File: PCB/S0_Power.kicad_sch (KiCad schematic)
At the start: 9 parts, among them J5 PJ-102BH, U10 LM2576HVS-5, U13 TLV76133DCY

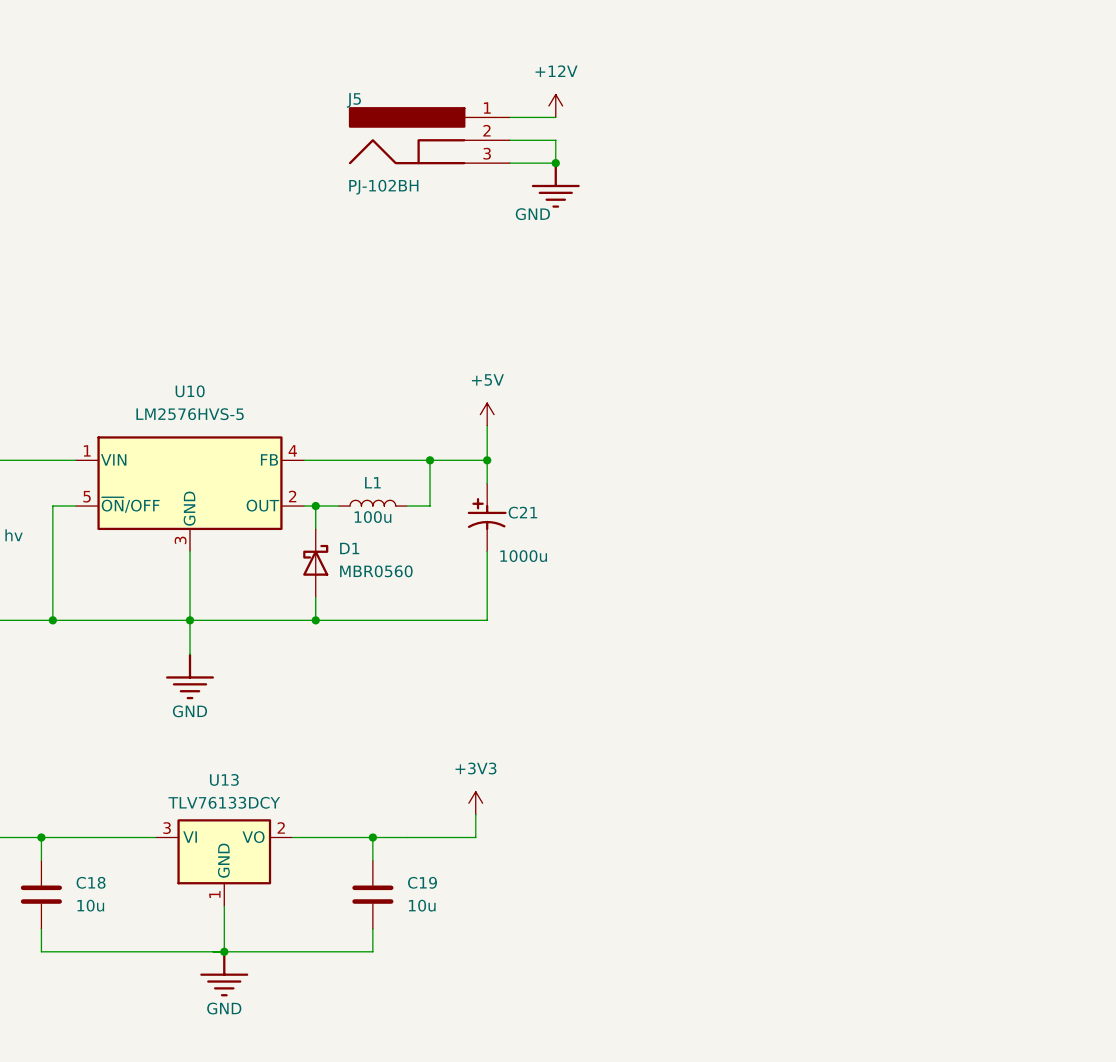
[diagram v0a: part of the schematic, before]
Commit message: Update PCB to seperate ground symbols apporiately. Modify board to sepearte ground path for motor current and all other devices. Add filtering for slide power, hopefully reduce bownout or other issue.
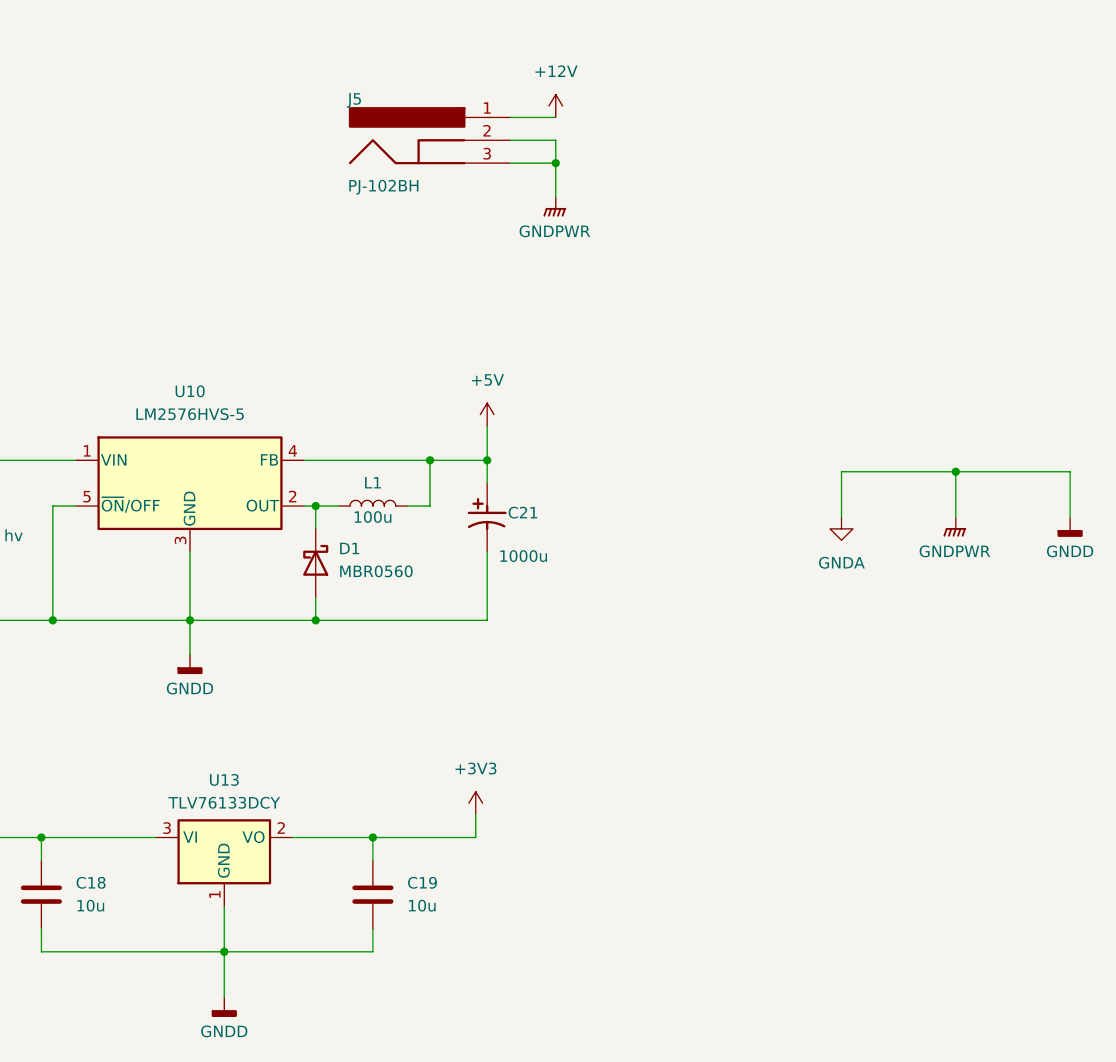
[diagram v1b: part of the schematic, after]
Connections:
- net GND renamed GNDA

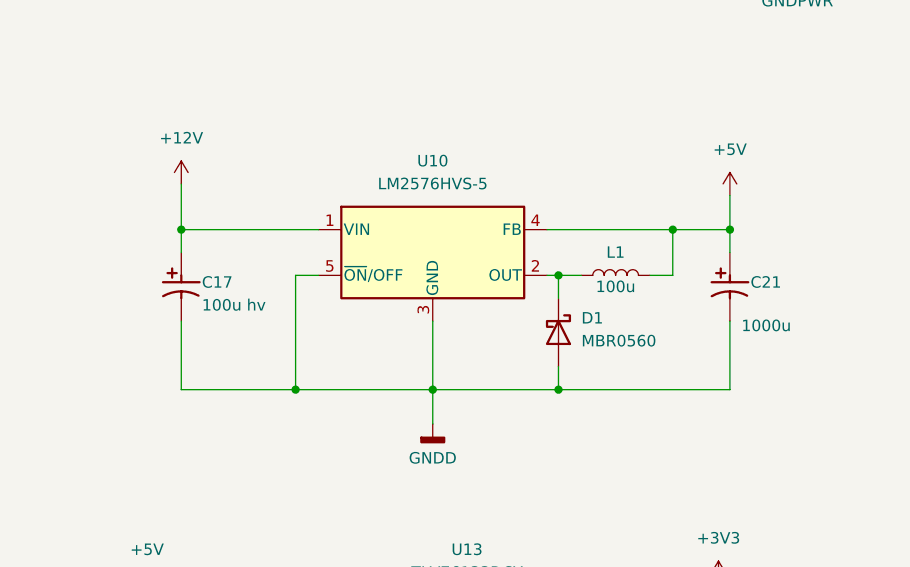
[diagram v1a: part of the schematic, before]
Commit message: WIP Adding adudino onboard, so far copying pro mega
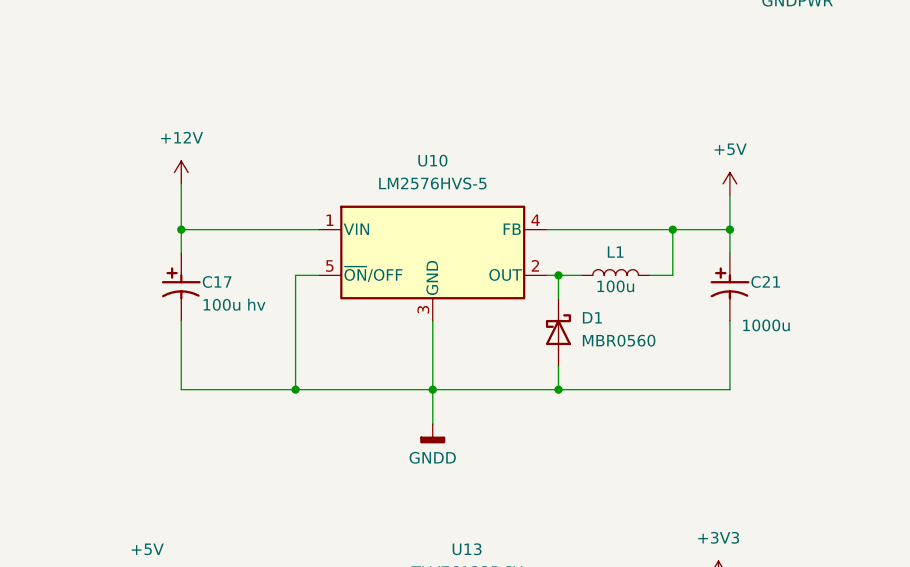
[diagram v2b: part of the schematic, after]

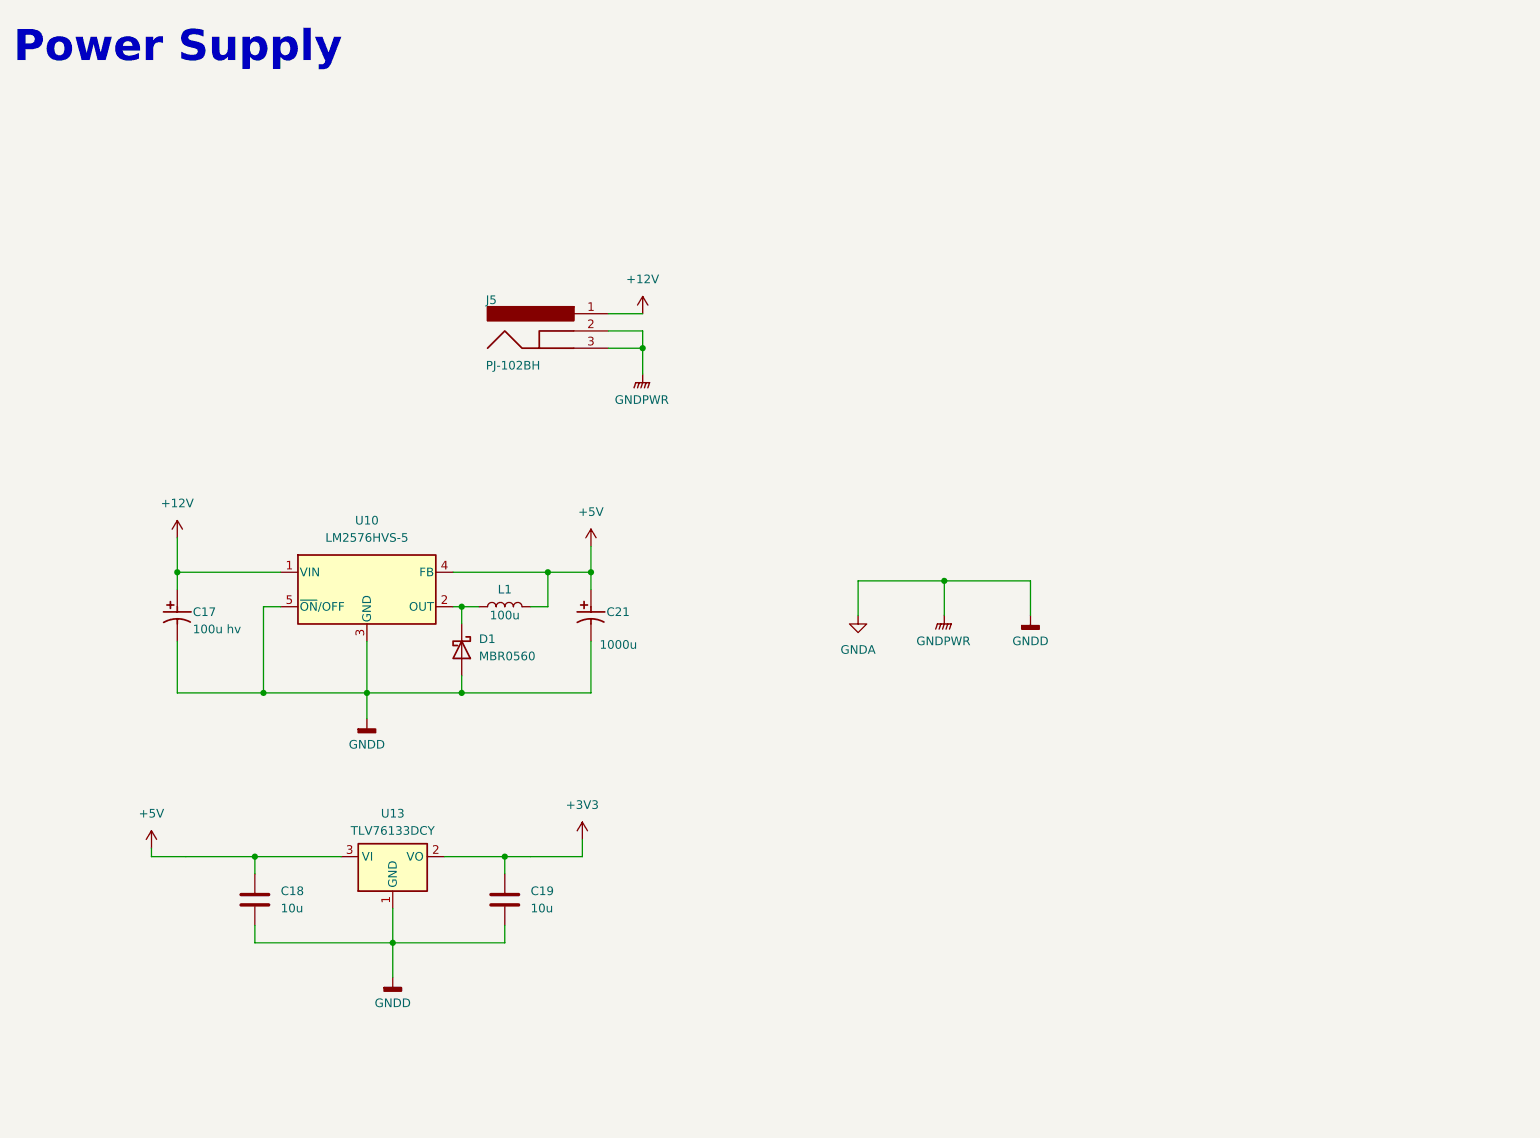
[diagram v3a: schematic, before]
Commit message: Changed power stage, there as a mistake, also generally changing lots of stuff
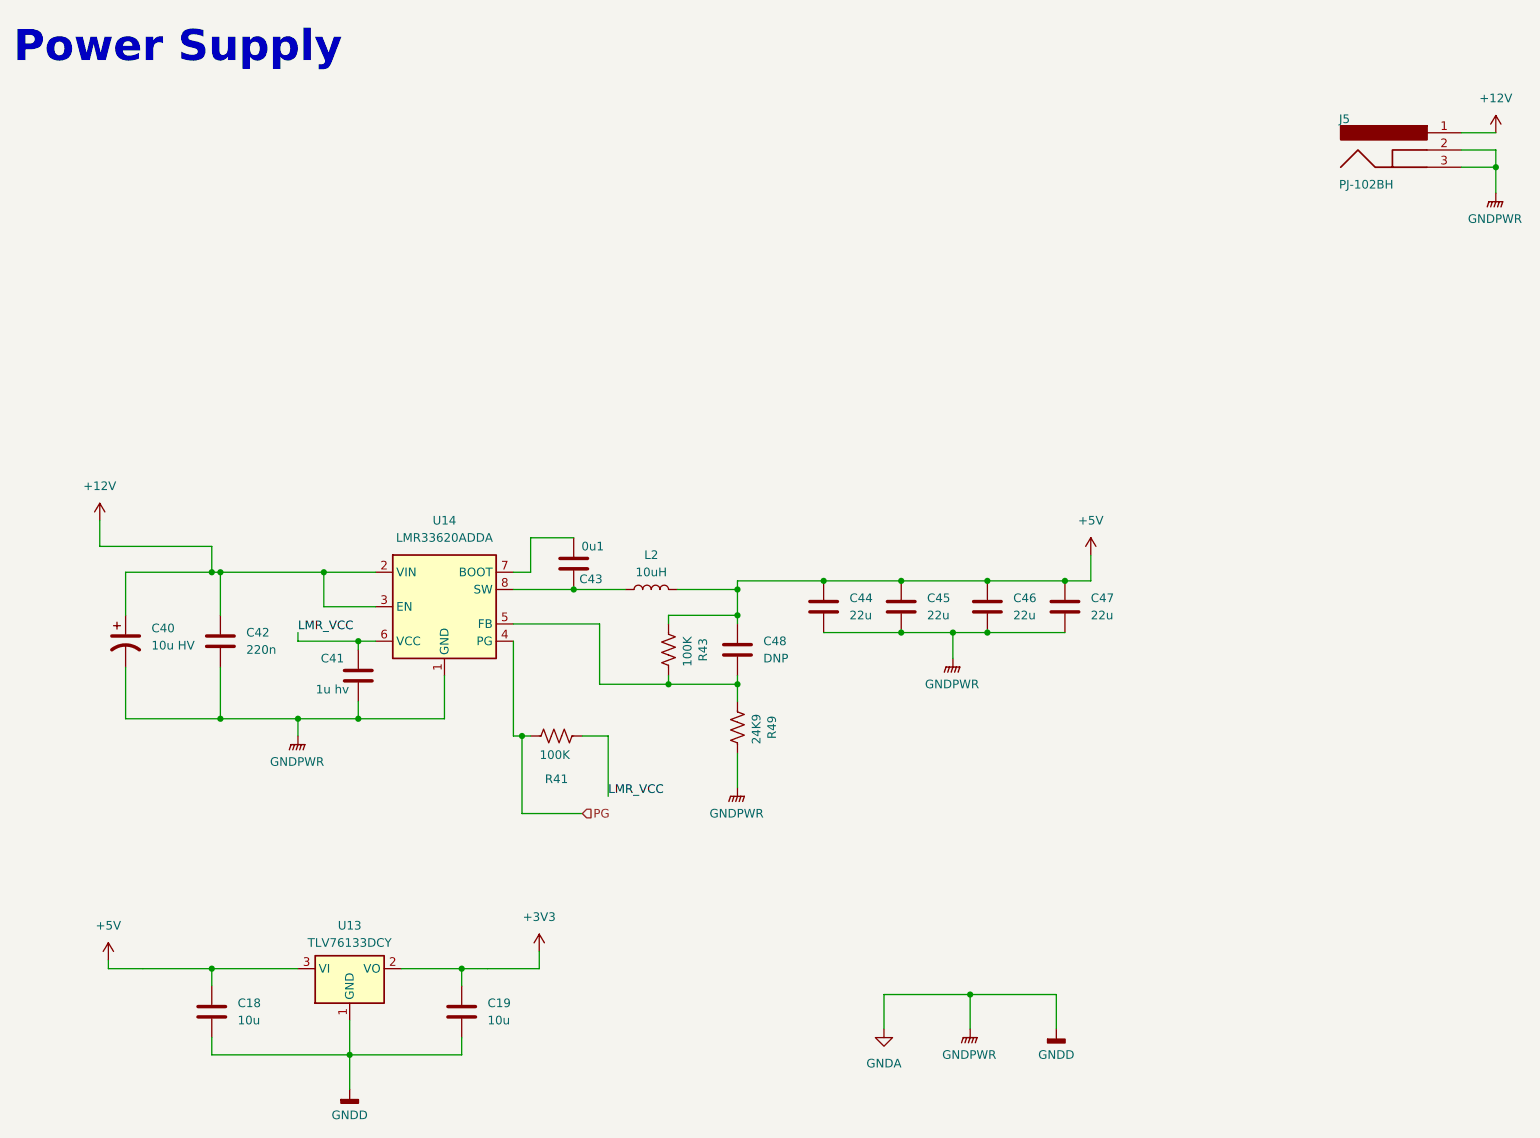
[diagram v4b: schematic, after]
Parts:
- removed C17: 100u hv, Capacitor_SMD:CP_Elec_10x10.5, symbol UMTK-altium-import:0_Polar Cap
- removed C21: 1000u, Capacitor_SMD:CP_Elec_8x10.5, symbol UMTK-altium-import:0_Polar Cap
- removed D1: MBR0560, Diode_SMD:D_SOD-123, symbol Diode:MBR0560
- removed L1: 100u, Inductor_SMD:L_Sunlord_MWSA1206S-101, symbol Device:L
- removed U10: LM2576HVS-5, Package_TO_SOT_SMD:TO-263-5_TabPin3, symbol Regulator_Switching:LM2576HVS-5
- added C40: 10u HV, symbol Device:C_Polarized_US
- added C41: 1u hv, Capacitor_SMD:C_0603_1608Metric, symbol Device:C
- added C42: 220n, symbol Device:C
- added C43: 0u1, Capacitor_SMD:C_0603_1608Metric, symbol Device:C
- added C44, C45, C46, C47: 22u, symbol Device:C
- added C48: DNP, Capacitor_SMD:C_1206_3216Metric, symbol Device:C
- added L2: 10uH, Inductor_SMD:L_Changjiang_FXL0530, symbol Device:L
- added R41, R43: 100K, Resistor_SMD:R_0603_1608Metric, symbol Device:R_US
- added R49: 24K9, symbol Device:R_US
- added U14: LMR33620ADDA, Package_SO:Texas_HSOP-8-1EP_3.9x4.9mm_P1.27mm_ThermalVias, symbol Regulator_Switching:LMR33620ADDA
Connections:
- net +12V: now also C40.1, C42.1, U14.2 (VIN), U14.3 (EN)
- net +5V: now also C44.1, C45.1, C46.1, C47.1, C48.2, L2.2, R43.2
- net GNDA: now also C40.2, C41.2, C42.2, C44.2, C45.2, C46.2, C47.2, R49.1, U14.1 (GND), U14.9 (GND)
- new net: C48.1, R43.1, R49.2, U14.5 (FB)
- new net: C43.2, U14.7 (BOOT)
- new net: C43.1, L2.1, U14.8 (SW)
- new net LMR_VCC: C41.1, R41.2, U14.6 (VCC)
- new net PG: R41.1, U14.4 (PG)
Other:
- moved on the sheet: C18, C19, J5, U13

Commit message: Update
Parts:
- removed C40: 10u HV, symbol Device:C_Polarized_US
- added C50: 10u HV, Capacitor_SMD:C_1210_3225Metric, symbol Device:C
- C42: footprint (none) -> Capacitor_SMD:C_0603_1608Metric
- C44, C45, C46, C47: footprint (none) -> Capacitor_SMD:C_1210_3225Metric
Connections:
- net +12V: now also C50.1
- net GNDA: now also C50.2
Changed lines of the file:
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@@
 			)
 		)
-		(property "Footprint" ""
+		(property "Footprint" "Capacitor_SMD:C_1210_3225Metric"
 			(at 171.1452 104.14 0)
 			(effects
@@
 				(path "/2bf3ea67-58b8-47b3-a768-ea6950b40edf/9034045e-70ca-44cd-84b0-62f91947c95b"
 					(reference "C47")
-					(unit 1)
-				)
-			)
-		)
-	)
-	(symbol
-		(lib_id "Device:C_Polarized_US")
-		(at 31.75 105.41 0)
-		(unit 1)
-		(exclude_from_sim no)
-		(in_bom yes)
-		(on_board yes)
-		(dnp no)
-		(fields_autoplaced yes)
-		(property "Reference" "C40"
-			(at 35.56 103.5049 0)
-			(effects
-				(font
-					(size 1.27 1.27)
-				)
-				(justify left)
-			)
-		)
-		(property "Value" "10u HV"
-			(at 35.56 106.0449 0)
-			(effects
-				(font
-					(size 1.27 1.27)
-				)
-				(justify left)
-			)
-		)
-		(property "Footprint" ""
-			(at 31.75 105.41 0)
-			(effects
-				(font
-					(size 1.27 1.27)
-				)
-				(hide yes)
-			)
-		)
-		(property "Datasheet" "~"
-			(at 31.75 105.41 0)
-			(effects
-				(font
-					(size 1.27 1.27)
-				)
-				(hide yes)
-			)
-		)
-		(property "Description" "Polarized capacitor, US symbol"
-			(at 31.75 105.41 0)
-			(effects
-				(font
-					(size 1.27 1.27)
-				)
-				(hide yes)
-			)
-		)
-		(pin "2"
-		)
-		(pin "1"
-		)
-		(instances
-			(project ""
-				(path "/2bf3ea67-58b8-47b3-a768-ea6950b40edf/9034045e-70ca-44cd-84b0-62f91947c95b"
-					(reference "C40")
 					(unit 1)
 				)
@@
 	)
 	(symbol
+		(lib_id "Device:C")
+		(at 31.75 105.41 0)
+		(unit 1)
+		(exclude_from_sim no)
+		(in_bom yes)
+		(on_board yes)
+		(dnp no)
+		(fields_autoplaced yes)
+		(property "Reference" "C50"
+			(at 35.56 104.1399 0)
+			(effects
+				(font
+					(size 1.27 1.27)
+				)
+				(justify left)
+			)
+		)
+		(property "Value" "10u HV"
+			(at 35.56 106.6799 0)
+			(effects
+				(font
+					(size 1.27 1.27)
+				)
+				(justify left)
+			)
+		)
+		(property "Footprint" "Capacitor_SMD:C_1210_3225Metric"
+			(at 32.7152 109.22 0)
+			(effects
+				(font
+					(size 1.27 1.27)
+				)
+				(hide yes)
+			)
+		)
+		(property "Datasheet" "~"
+			(at 31.75 105.41 0)
+			(effects
+				(font
+					(size 1.27 1.27)
+				)
+				(hide yes)
+			)
+		)
+		(property "Description" "Unpolarized capacitor"
+			(at 31.75 105.41 0)
+			(effects
+				(font
+					(size 1.27 1.27)
+				)
+				(hide yes)
+			)
+		)
+		(pin "1"
+		)
+		(pin "2"
+		)
+		(instances
+			(project "UMTK"
+				(path "/2bf3ea67-58b8-47b3-a768-ea6950b40edf/9034045e-70ca-44cd-84b0-62f91947c95b"
+					(reference "C50")
+					(unit 1)
+				)
+			)
+		)
+	)
+	(symbol
 		(lib_id "Device:R_US")
 		(at 111.76 106.68 180)
@@
 			)
 		)
-		(property "Footprint" ""
+		(property "Footprint" "Capacitor_SMD:C_0603_1608Metric"
 			(at 46.6852 109.22 0)
 			(effects
@@
 			)
 		)
-		(property "Footprint" ""
+		(property "Footprint" "Capacitor_SMD:C_1210_3225Metric"
 			(at 135.5852 104.14 0)
 			(effects
@@
 			)
 		)
-		(property "Footprint" ""
+		(property "Footprint" "Capacitor_SMD:C_1210_3225Metric"
 			(at 147.0152 104.14 0)
 			(effects
@@
 			)
 		)
-		(property "Footprint" ""
+		(property "Footprint" "Capacitor_SMD:C_1210_3225Metric"
 			(at 159.7152 104.14 0)
 			(effects

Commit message: Laying out
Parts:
- C48: footprint Capacitor_SMD:C_1206_3216Metric -> Capacitor_SMD:C_0603_1608Metric
- L2: footprint Inductor_SMD:L_Changjiang_FXL0530 -> Inductor_SMD:L_Changjiang_FXL0630
- R49: footprint (none) -> Resistor_SMD:R_0603_1608Metric
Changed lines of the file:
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@@
 			)
 		)
-		(property "Footprint" "Inductor_SMD:L_Changjiang_FXL0530"
+		(property "Footprint" "Inductor_SMD:L_Changjiang_FXL0630"
 			(at 109.22 97.79 0)
 			(effects
@@
 			)
 		)
-		(property "Footprint" ""
+		(property "Footprint" "Resistor_SMD:R_0603_1608Metric"
 			(at 120.904 117.856 90)
 			(effects
@@
 			)
 		)
-		(property "Footprint" "Capacitor_SMD:C_1206_3216Metric"
+		(property "Footprint" "Capacitor_SMD:C_0603_1608Metric"
 			(at 120.9548 102.87 0)
 			(effects
